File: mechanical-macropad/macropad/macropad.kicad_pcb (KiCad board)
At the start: 2 copper layers, 76 x 176.4 mm, 84 parts, among them J1 USB_B_Micro, J2 AVR-ISP-6, K1 KEYSW, K10 KEYSW, K11 KEYSW, K12 KEYSW, K13 KEYSW, K14 KEYSW, K15 KEYSW, K16 KEYSW, K17 KEYSW, K18 KEYSW, K19 KEYSW, K2 KEYSW, K20 KEYSW, K21 KEYSW, K22 KEYSW, K23 KEYSW, K24 KEYSW, K25 KEYSW, K26 KEYSW, K27 KEYSW, K28 KEYSW, K3 KEYSW, K4 KEYSW, K5 KEYSW, K6 KEYSW, K7 KEYSW, K8 KEYSW, K9 KEYSW, SW1 SW_Push, U1 ATMEGA32U4, X1 XTAL_GND

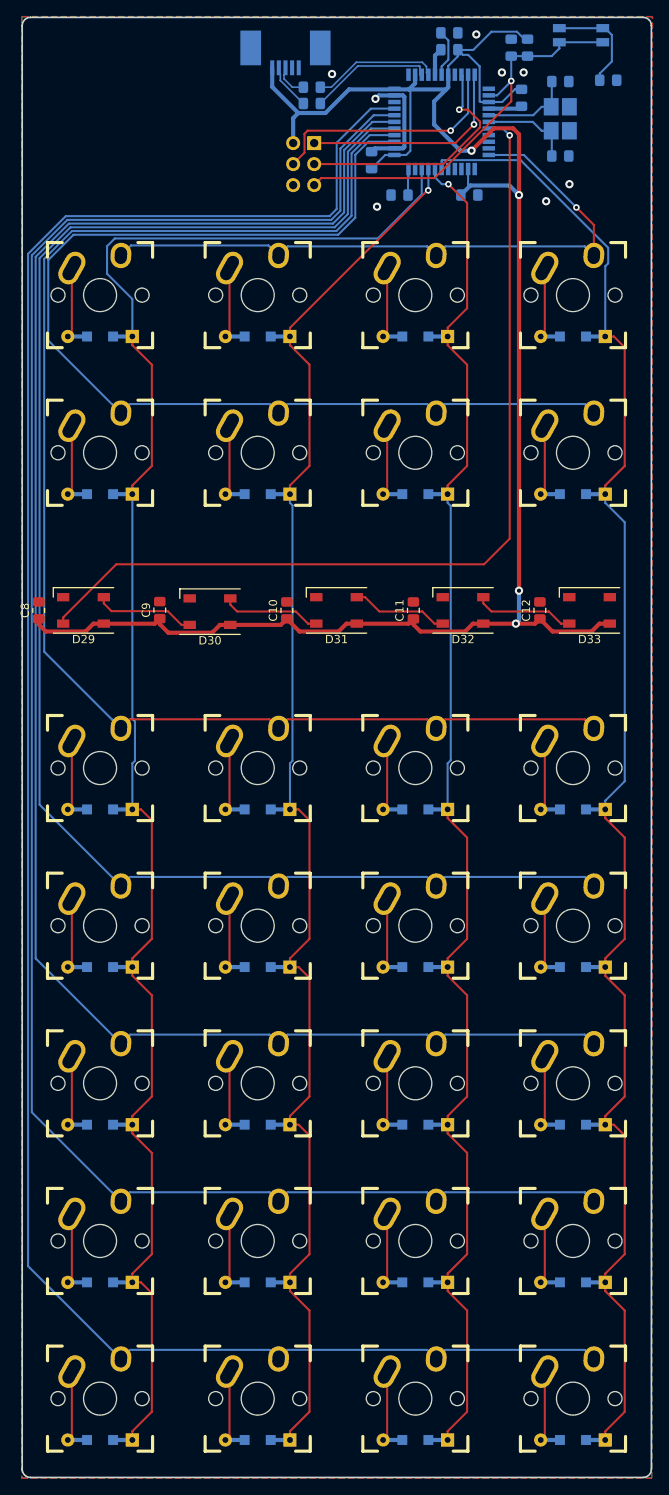
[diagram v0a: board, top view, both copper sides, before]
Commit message: improve groundplanes, reroute
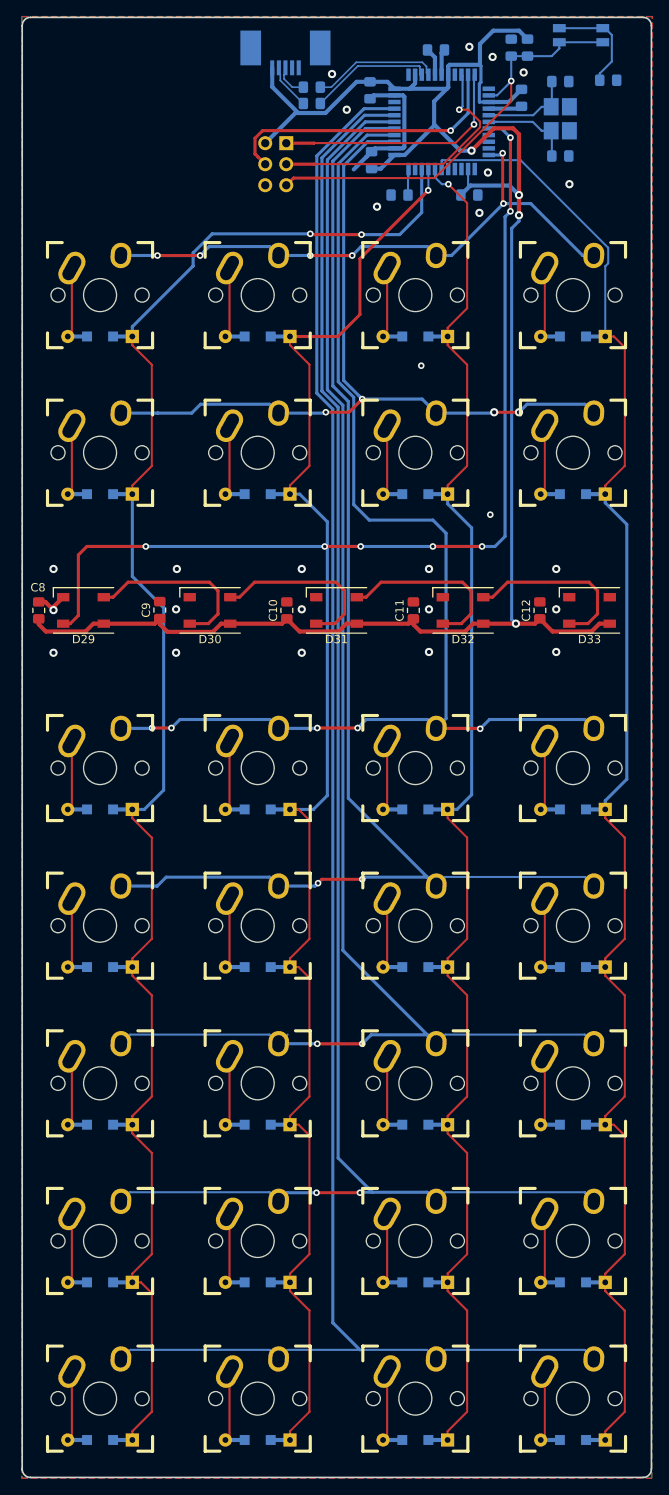
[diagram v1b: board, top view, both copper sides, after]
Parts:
- moved C7 10.8 mm to (157.5, 84.9), turned to 270 degrees
- moved J2 3.38 mm to (147.4, 91.3)
- moved C3 2.62 mm to (165.5, 80.1), turned to 0 degrees
- moved D30 0.15 mm to (138.2, 147.8)
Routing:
- net Row7: track 254.3 -> 218.1 mm
- net Row2: track 134.2 -> 98.3 mm, vias 0 -> 4
- net Row6: track 233.9 -> 199.9 mm, vias 0 -> 2
- net Row4: track 193.6 -> 161.7 mm, vias 0 -> 2
- net Row5: track 213.8 -> 183.7 mm, vias 0 -> 2
- net Row3: track 173.4 -> 146.7 mm, vias 0 -> 5
- net Net-(D31-Pad4): track 11.7 -> 21.7 mm
- net Net-(D30-Pad4): track 12.1 -> 21.7 mm
- net Net-(D32-Pad4): track 12.2 -> 21.7 mm
- net Net-(D29-Pad4): track 12.2 -> 21.7 mm
- net Col2: track 172.4 -> 181.7 mm
- net GND: track 21.4 -> 29.4 mm, vias 8 -> 26
- net Row1: track 79.9 -> 72.0 mm, vias 1 -> 6
- net /ISP_MOSI: track 29.7 -> 35.3 mm
- net Col1: track 200.5 -> 195.8 mm, vias 0 -> 2
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
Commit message: Add debug LED, debug pads, reroute
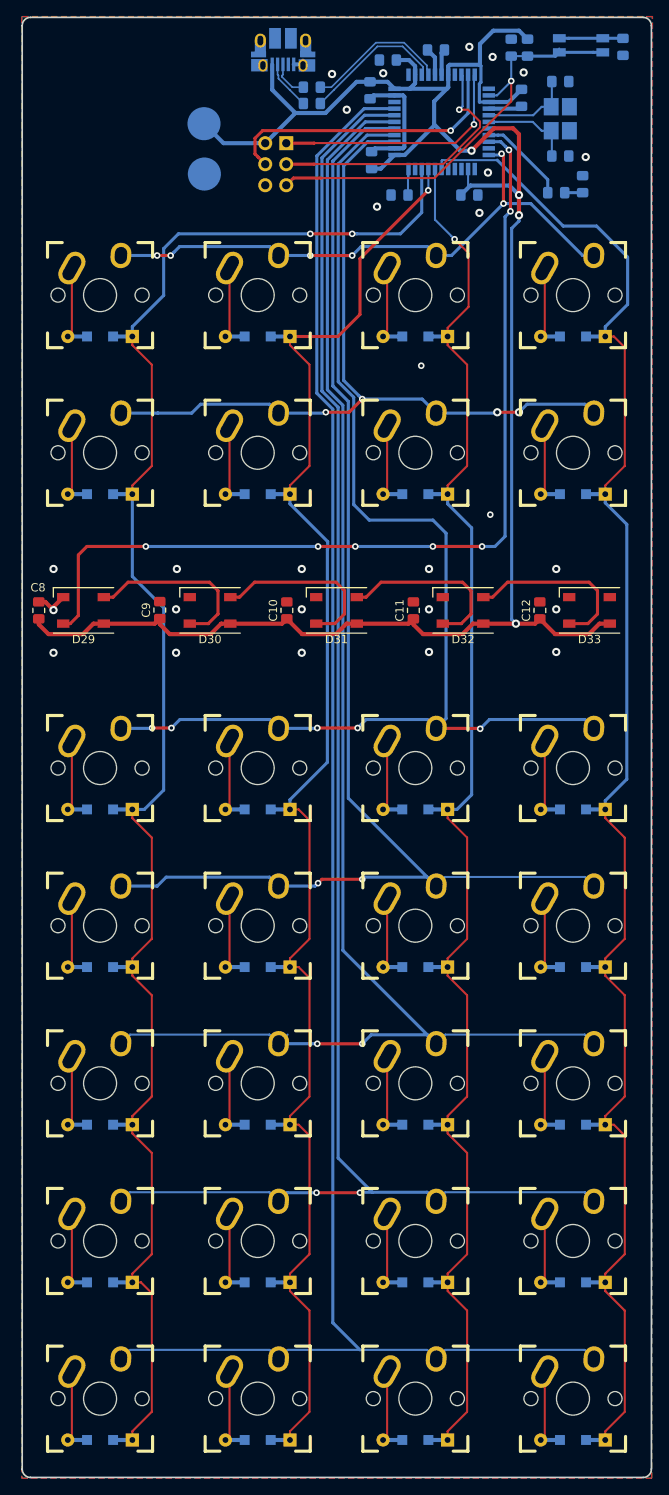
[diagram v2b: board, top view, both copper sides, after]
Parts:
- added C14: 0.1u, Capacitor_SMD:C_0805_2012Metric_Pad1.15x1.40mm_HandSolder, B.Cu at (159.7, 81.3)
- added D34: LED, LED_SMD:LED_0805_2012Metric_Pad1.15x1.40mm_HandSolder, B.Cu at (180.0, 97.3)
- added R6: 150R, Resistor_SMD:R_0805_2012Metric_Pad1.15x1.40mm_HandSolder, B.Cu at (183.2, 96.3)
- added TP1: 5V0, TestPoint:TestPoint_Pad_D4.0mm, B.Cu at (137.4, 89.0)
- added TP2: GND, TestPoint:TestPoint_Pad_D4.0mm, B.Cu at (137.5, 95.1)
- J1: footprint keyboard_parts:USB_miniB_hirose_5ST_hand -> Connector_USB:USB_Micro-B_Amphenol_10103594-0001LF_Horizontal
- moved R5 4.41 mm to (188.1, 79.7), turned to 270 degrees
- moved J1 2.20 mm to (147.0, 80.0)
- moved SW1 1.22 mm to (183.0, 79.5)
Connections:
- U1 pad 18: /NEOPIXEL_IN -> Net-(U1-Pad18)
- U1 pad 19: Net-(U1-Pad19) -> /DBG_LED
- U1 pad 20: Net-(U1-Pad20) -> /NEOPIXEL_IN
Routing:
- net VCC: track 236.6 -> 250.1 mm
- net /DBG_LED: track 0.00 -> 10.9 mm
- net Net-(R5-Pad1): track 12.8 -> 7.69 mm
- net Col4: track 182.9 -> 185.6 mm
- net Col2: track 181.7 -> 179.4 mm
- net Col1: track 195.8 -> 198.1 mm
- net /MCU_D-: track 15.1 -> 17.3 mm
- net Net-(D34-Pad1): track 0.00 -> 2.17 mm
- net /MCU_D+: track 15.4 -> 17.4 mm
- net GND: track 29.4 -> 27.7 mm, vias 26 -> 27
- net /NEOPIXEL_IN: track 113.6 -> 111.9 mm
- net /ISP_RESET: track 52.6 -> 51.7 mm
